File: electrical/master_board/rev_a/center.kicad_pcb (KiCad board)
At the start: 2 copper layers, 125 x 97.6 mm, 7 parts, among them CN50 HCSR04;F1X4, CN51 HCSR04LP;F1X4, CN52 HCSR04LP;F1X4, CN53 HCSR04LP;F1X4, CN54 HCSR04;F1X4, CN55 HR2_EncoderMate;2XF1X3, CN56 HR2_EncoderMate;2XF1X3

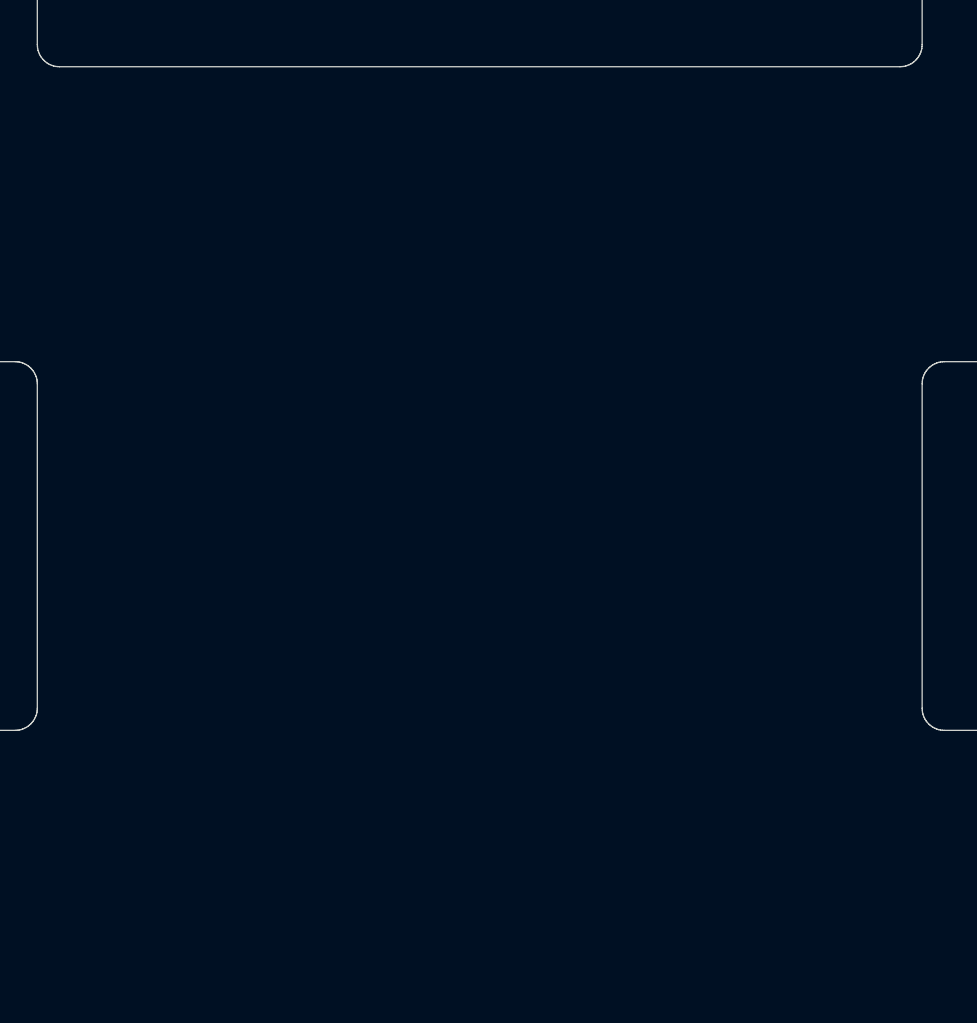
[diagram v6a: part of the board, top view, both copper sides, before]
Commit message: Did initial placement of RasPi4B+ (at origin).
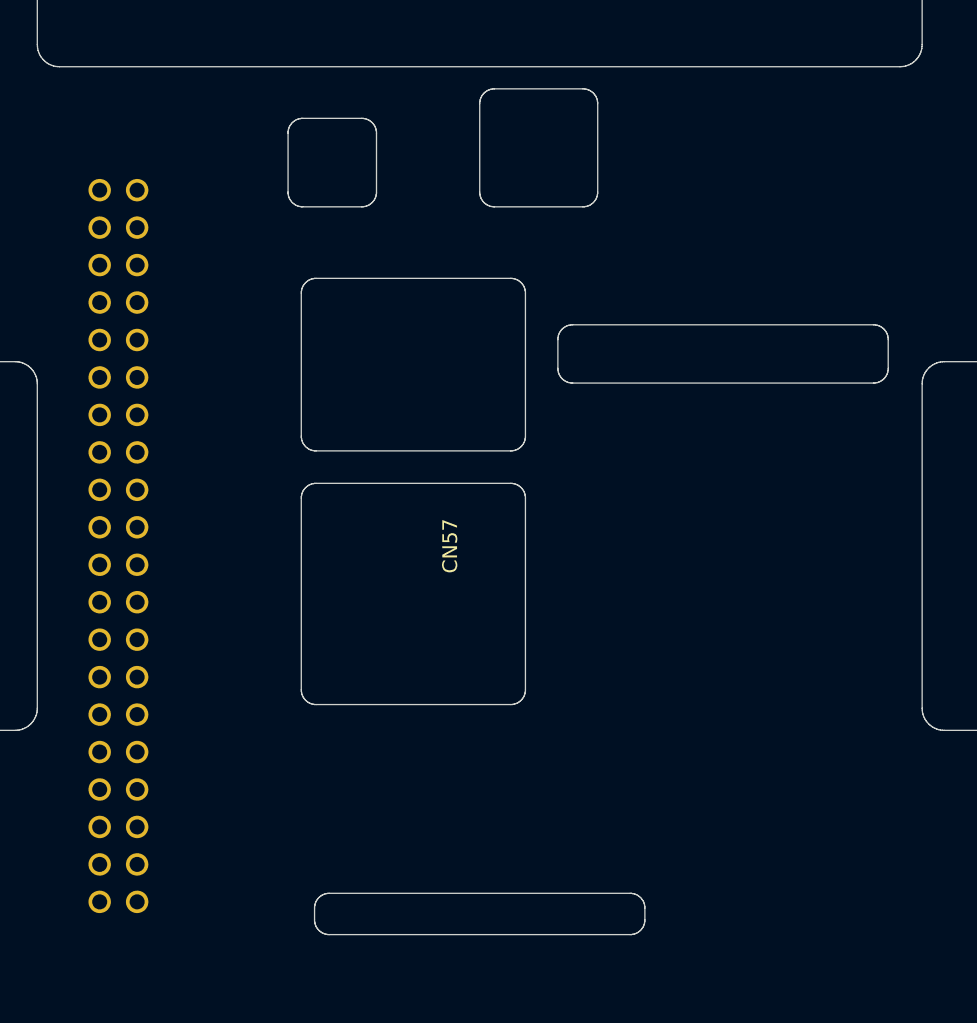
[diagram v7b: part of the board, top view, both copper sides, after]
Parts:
- added CN57: RASPI;F2X20, HR2:RASPI_F2X20, F.Cu at (100.0, 100.0)
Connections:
- CN51 pad 1: (no net) -> Net-(CN51-Pad1)
- CN51 pad 2: (no net) -> Net-(CN51-Pad2)
- CN51 pad 3: (no net) -> Net-(CN51-Pad3)
- CN51 pad 4: (no net) -> Net-(CN51-Pad4)
- CN52 pad 1: (no net) -> Net-(CN52-Pad1)
- CN52 pad 2: (no net) -> Net-(CN52-Pad2)
- CN52 pad 3: (no net) -> Net-(CN52-Pad3)
- CN52 pad 4: (no net) -> Net-(CN52-Pad4)
- CN53 pad 1: (no net) -> Net-(CN53-Pad1)
- CN53 pad 2: (no net) -> Net-(CN53-Pad2)
- CN53 pad 3: (no net) -> Net-(CN53-Pad3)
- CN53 pad 4: (no net) -> Net-(CN53-Pad4)
- CN55 pad 1: (no net) -> Net-(CN55-Pad1)
- CN55 pad 2: (no net) -> Net-(CN55-Pad2)
- CN55 pad 3: (no net) -> Net-(CN55-Pad3)
- CN55 pad 4: (no net) -> Net-(CN55-Pad4)
- CN55 pad 5: (no net) -> Net-(CN55-Pad5)
- CN55 pad 6: (no net) -> Net-(CN55-Pad6)
- CN56 pad 1: (no net) -> Net-(CN56-Pad1)
- CN56 pad 2: (no net) -> Net-(CN56-Pad2)
- CN56 pad 3: (no net) -> Net-(CN56-Pad3)
- CN56 pad 4: (no net) -> Net-(CN56-Pad4)
- CN56 pad 5: (no net) -> Net-(CN56-Pad5)
- CN56 pad 6: (no net) -> Net-(CN56-Pad6)
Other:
- outline, holes or cut-outs redrawn

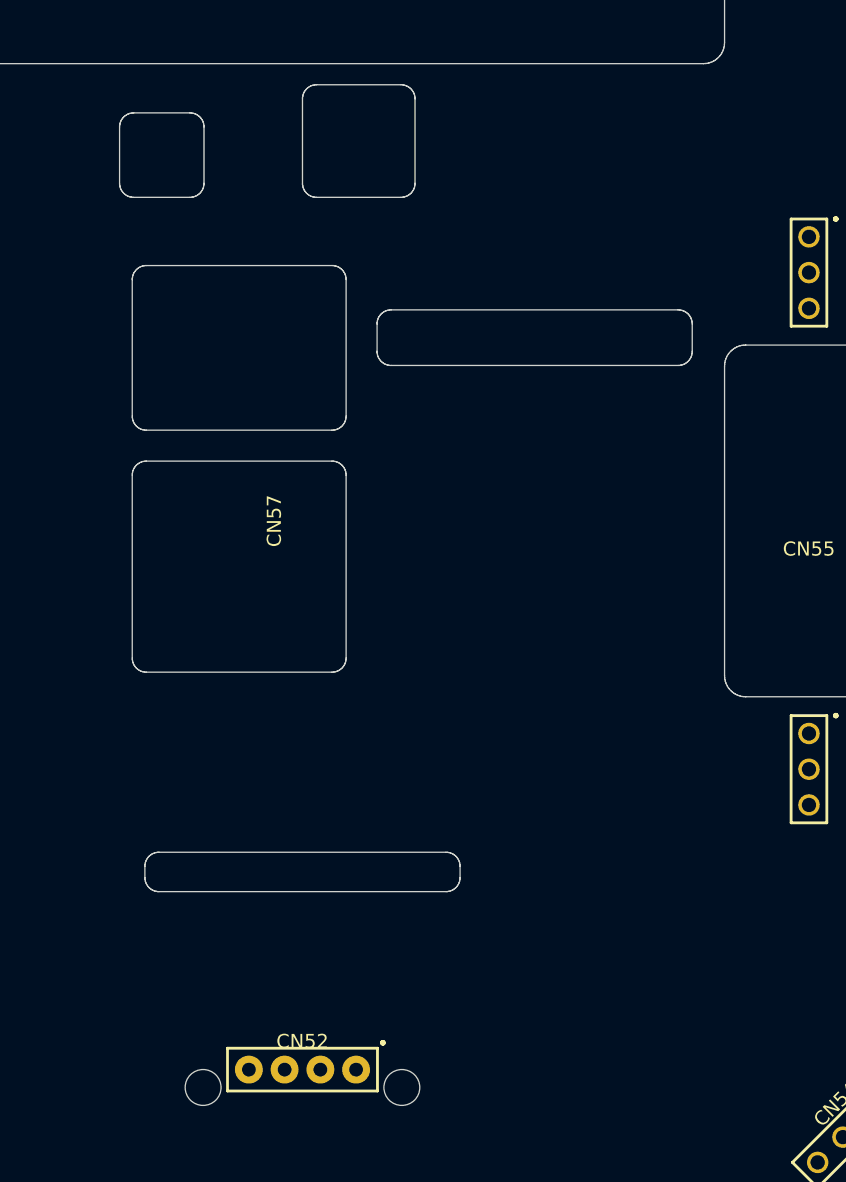
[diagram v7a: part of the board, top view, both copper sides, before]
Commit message: Added .../st_adaptor/rev_a directory.  ST_MATE is properly integrated as a symbol/footprint.
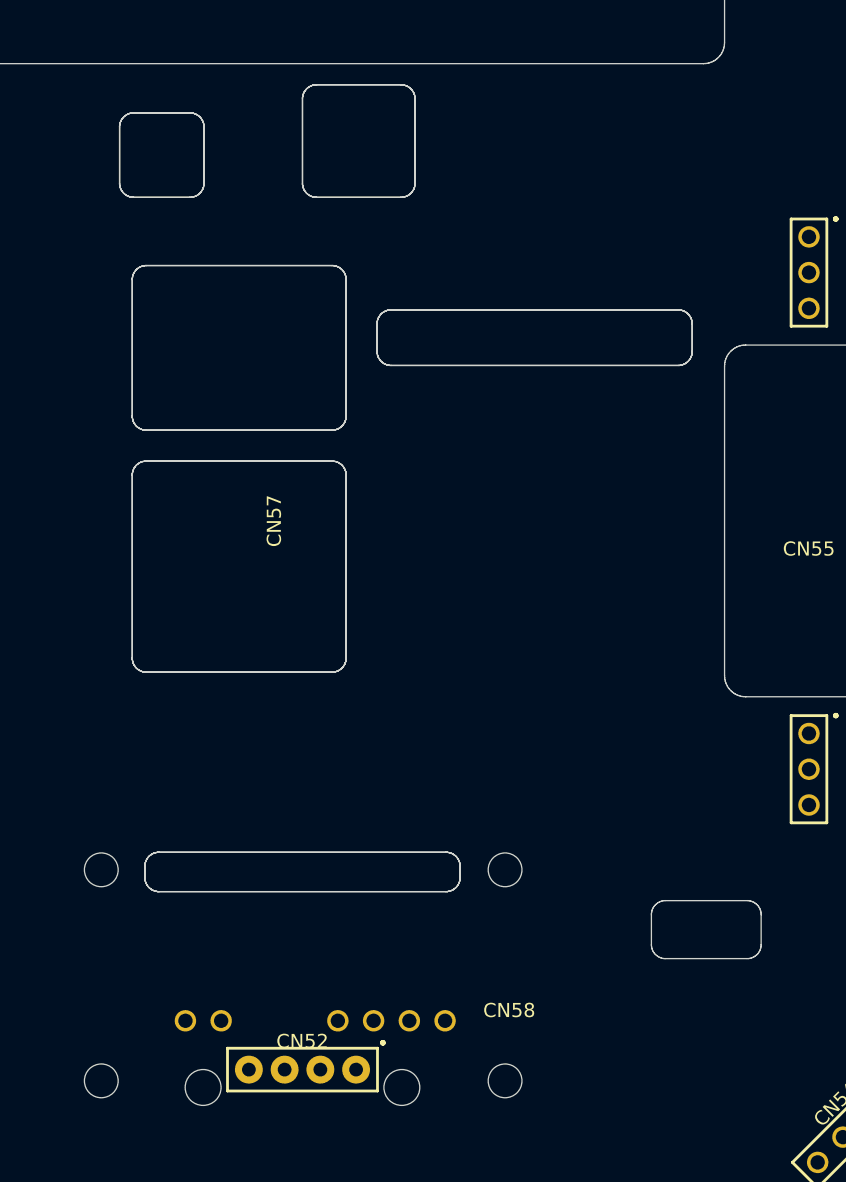
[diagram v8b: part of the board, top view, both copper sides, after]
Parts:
- added CN58: ST_MATE;ST_MATE, HR2:ST_MATE, F.Cu at (114.7, 136.8)
